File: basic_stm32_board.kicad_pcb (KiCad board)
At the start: 4 copper layers, 2 x 7.5 mm, 61 parts, among them J1 Screw_Terminal_01x02, J2 USB_B_Micro, J3 Conn_01x04, J4 Conn_01x04, J5 Conn_ARM_JTAG_SWD_10, Q1 AO3401A, SW1 SW_SPDT, U1 STM32F405RGT6, U2 MP2303ADN, U3 USBLC6-2SC6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

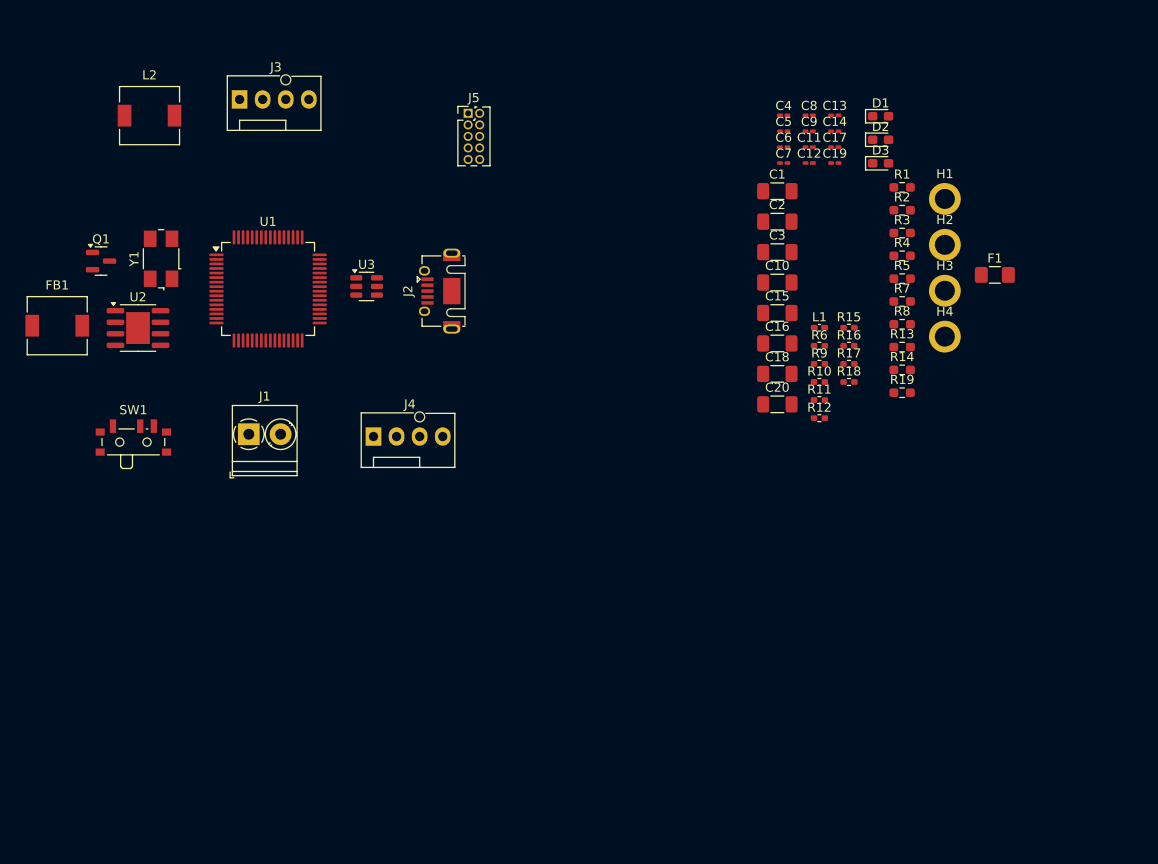
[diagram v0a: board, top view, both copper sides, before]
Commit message: changed some footprints
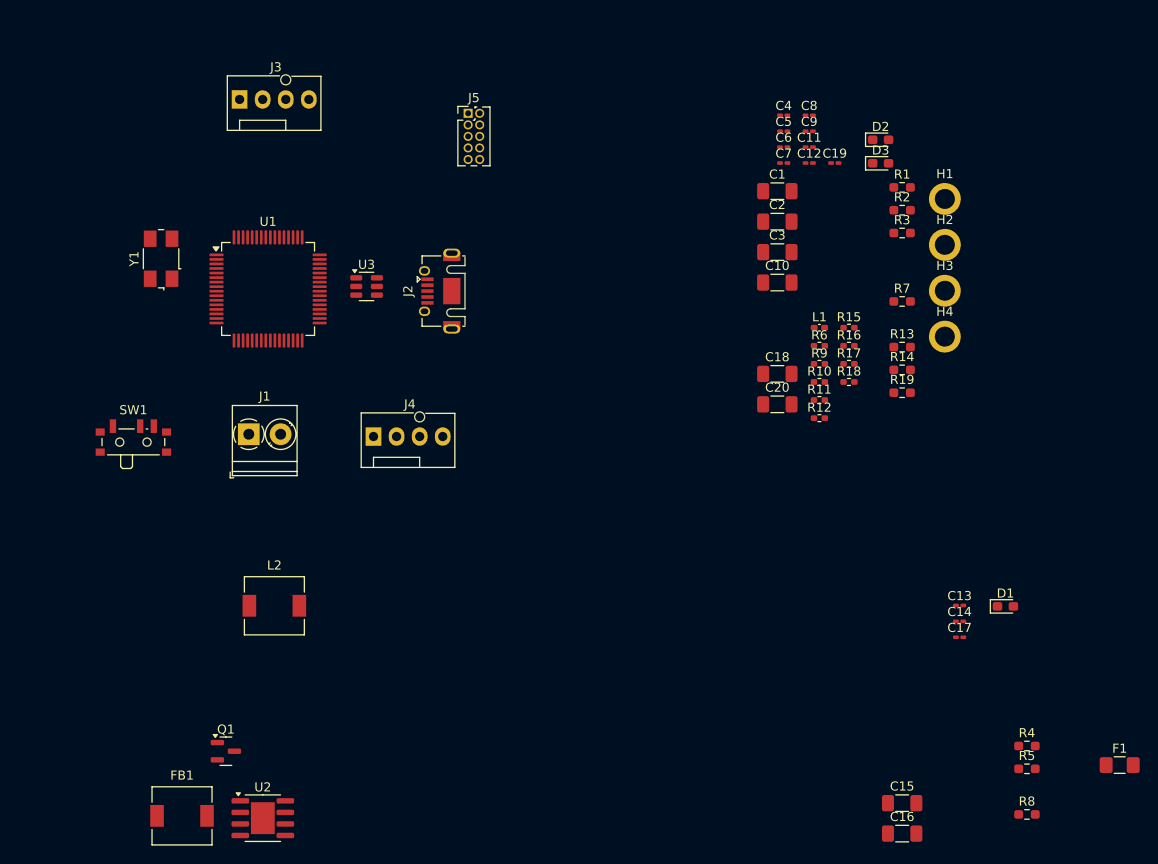
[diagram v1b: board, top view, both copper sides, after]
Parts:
- moved U2 55.6 mm to (156.2, 155.0)
- moved C13 55.6 mm to (232.9, 131.6)
- moved C14 55.6 mm to (232.9, 133.4)
- moved C15 55.6 mm to (226.6, 153.4)
- moved C17 55.6 mm to (232.9, 135.1)
- moved F1 55.6 mm to (250.5, 149.2)
- moved FB1 55.6 mm to (147.3, 154.8)
- moved Q1 55.6 mm to (152.2, 147.7)
- moved R4 55.6 mm to (240.3, 147.1)
- moved R5 55.6 mm to (240.3, 149.6)
- moved R8 55.6 mm to (240.3, 154.6)
- moved C16 55.6 mm to (226.6, 156.7)
- moved D1 55.6 mm to (237.9, 131.7)
- moved L2 55.6 mm to (157.5, 131.7)
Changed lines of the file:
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@@
 	(footprint "Inductor_SMD:L_6.3x6.3_H3"
 		(layer "F.Cu")
-		(at 133.604 100.838)
+		(at 147.3375 154.766)
 		(descr "Choke, SMD, 6.3x6.3mm 3mm height")
 		(tags "Choke SMD")
@@
 	(footprint "Inductor_SMD:L_6.3x6.3_H3"
 		(layer "F.Cu")
-		(at 143.764 77.724)
+		(at 157.4975 131.652)
 		(descr "Choke, SMD, 6.3x6.3mm 3mm height")
 		(tags "Choke SMD")
@@
 		(tags "Micro AB USB SMD")
 		(property "Reference" "J2"
-			(at 0 -4.8 270)
+			(at 0 -4.8 -90)
 			(layer "F.SilkS")
 			(effects
@@
 		)
 		(property "Value" "USB_B_Micro"
-			(at 0 3.5 270)
+			(at 0 3.5 -90)
 			(layer "F.Fab")
 			(effects
@@
 		)
 		(fp_text user "PCB Edge"
-			(at 0 1.45 270)
+			(at 0 1.45 -90)
 			(layer "Dwgs.User")
 			(effects
@@
 		)
 		(fp_text user "${REFERENCE}"
-			(at 0 -1.5 270)
+			(at 0 -1.5 -90)
 			(layer "F.Fab")
 			(effects
@@
 	(footprint "Capacitor_SMD:C_1206_3216Metric_Pad1.33x1.80mm_HandSolder"
 		(layer "F.Cu")
-		(at 212.8345 102.79)
+		(at 226.568 156.718)
 		(descr "Capacitor SMD 1206 (3216 Metric), square (rectangular) end terminal, IPC_7351 nominal with elongated pad for handsoldering. (Body size source: IPC-SM-782 page 76, https://www.pcb-3d.com/wordpress/wp-content/uploads/ipc-sm-782a_amendment_1_and_2.pdf), generated with kicad-footprint-generator")
 		(tags "capacitor handsolder")
@@
 	(footprint "Capacitor_SMD:C_0201_0603Metric_Pad0.64x0.40mm_HandSolder"
 		(layer "F.Cu")
-		(at 219.1545 77.69)
+		(at 232.888 131.618)
 		(descr "Capacitor SMD 0201 (0603 Metric), square (rectangular) end terminal, IPC_7351 nominal with elongated pad for handsoldering. (Body size source: https://www.vishay.com/docs/20052/crcw0201e3.pdf), generated with kicad-footprint-generator")
 		(tags "capacitor handsolder")
@@
 		(tags "SMD SMT crystal")
 		(property "Reference" "Y1"
-			(at 0 -2.95 270)
+			(at 0 -2.95 -90)
 			(layer "F.SilkS")
 			(effects
@@
 		)
 		(property "Value" "16MHz"
-			(at 0 2.95 270)
+			(at 0 2.95 -90)
 			(layer "F.Fab")
 			(effects
@@
 		)
 		(fp_text user "${REFERENCE}"
-			(at 0 0 270)
+			(at 0 0 -90)
 			(layer "F.Fab")
 			(effects
@@
 	(footprint "Capacitor_SMD:C_1206_3216Metric_Pad1.33x1.80mm_HandSolder"
 		(layer "F.Cu")
-		(at 212.8345 99.44)
+		(at 226.568 153.368)
 		(descr "Capacitor SMD 1206 (3216 Metric), square (rectangular) end terminal, IPC_7351 nominal with elongated pad for handsoldering. (Body size source: IPC-SM-782 page 76, https://www.pcb-3d.com/wordpress/wp-content/uploads/ipc-sm-782a_amendment_1_and_2.pdf), generated with kicad-footprint-generator")
 		(tags "capacitor handsolder")
@@
 	(footprint "Resistor_SMD:R_0603_1608Metric_Pad0.98x0.95mm_HandSolder"
 		(layer "F.Cu")
-		(at 226.5645 100.68)
+		(at 240.298 154.608)
 		(descr "Resistor SMD 0603 (1608 Metric), square (rectangular) end terminal, IPC_7351 nominal with elongated pad for handsoldering. (Body size source: IPC-SM-782 page 72, https://www.pcb-3d.com/wordpress/wp-content/uploads/ipc-sm-782a_amendment_1_and_2.pdf), generated with kicad-footprint-generator")
 		(tags "resistor handsolder")
@@
 	(footprint "Resistor_SMD:R_0603_1608Metric_Pad0.98x0.95mm_HandSolder"
 		(layer "F.Cu")
-		(at 226.5645 93.15)
+		(at 240.298 147.078)
 		(descr "Resistor SMD 0603 (1608 Metric), square (rectangular) end terminal, IPC_7351 nominal with elongated pad for handsoldering. (Body size source: IPC-SM-782 page 72, https://www.pcb-3d.com/wordpress/wp-content/uploads/ipc-sm-782a_amendment_1_and_2.pdf), generated with kicad-footprint-generator")
 		(tags "resistor handsolder")
@@
 	(footprint "Package_TO_SOT_SMD:SOT-23"
 		(layer "F.Cu")
-		(at 138.43 93.726)
+		(at 152.1635 147.654)
 		(descr "SOT, 3 Pin (https://www.jedec.org/system/files/docs/to-236h.pdf variant AB), generated with kicad-footprint-generator ipc_gullwing_generator.py")
 		(tags "SOT TO_SOT_SMD")
@@
 	(footprint "Diode_SMD:D_0603_1608Metric_Pad1.05x0.95mm_HandSolder"
 		(layer "F.Cu")
-		(at 224.1995 77.79)
+		(at 237.933 131.718)
 		(descr "Diode SMD 0603 (1608 Metric), square (rectangular) end terminal, IPC_7351 nominal, (Body size source: http://www.tortai-tech.com/upload/download/2011102023233369053.pdf), generated with kicad-footprint-generator")
 		(tags "diode handsolder")
@@
 	(footprint "Fuse:Fuse_1206_3216Metric_Pad1.42x1.75mm_HandSolder"
 		(layer "F.Cu")
-		(at 236.7645 95.25)
+		(at 250.498 149.178)
 		(descr "Fuse SMD 1206 (3216 Metric), square (rectangular) end terminal, IPC_7351 nominal with elongated pad for handsoldering. (Body size source: http://www.tortai-tech.com/upload/download/2011102023233369053.pdf), generated with kicad-footprint-generator")
 		(tags "fuse handsolder")
@@
 	(footprint "Resistor_SMD:R_0603_1608Metric_Pad0.98x0.95mm_HandSolder"
 		(layer "F.Cu")
-		(at 226.5645 95.66)
+		(at 240.298 149.588)
 		(descr "Resistor SMD 0603 (1608 Metric), square (rectangular) end terminal, IPC_7351 nominal with elongated pad for handsoldering. (Body size source: IPC-SM-782 page 72, https://www.pcb-3d.com/wordpress/wp-content/uploads/ipc-sm-782a_amendment_1_and_2.pdf), generated with kicad-footprint-generator")
 		(tags "resistor handsolder")
@@
 	(footprint "Capacitor_SMD:C_0201_0603Metric_Pad0.64x0.40mm_HandSolder"
 		(layer "F.Cu")
-		(at 219.1545 81.19)
+		(at 232.888 135.118)
 		(descr "Capacitor SMD 0201 (0603 Metric), square (rectangular) end terminal, IPC_7351 nominal with elongated pad for handsoldering. (Body size source: https://www.vishay.com/docs/20052/crcw0201e3.pdf), generated with kicad-footprint-generator")
 		(tags "capacitor handsolder")
@@
 	(footprint "Capacitor_SMD:C_0201_0603Metric_Pad0.64x0.40mm_HandSolder"
 		(layer "F.Cu")
-		(at 219.1545 79.44)
+		(at 232.888 133.368)
 		(descr "Capacitor SMD 0201 (0603 Metric), square (rectangular) end terminal, IPC_7351 nominal with elongated pad for handsoldering. (Body size source: https://www.vishay.com/docs/20052/crcw0201e3.pdf), generated with kicad-footprint-generator")
 		(tags "capacitor handsolder")
@@
 	(footprint "Package_SO:SOIC-8-1EP_3.9x4.9mm_P1.27mm_EP2.62x3.51mm"
 		(layer "F.Cu")
-		(at 142.494 101.092)
+		(at 156.2275 155.02)
 		(descr "SOIC, 8 Pin (https://www.monolithicpower.com/en/documentview/productdocument/index/version/2/document_type/Datasheet/lang/en/sku/MP2303A/document_id/494#page=14), generated with kicad-footprint-generator ipc_gullwing_generator.py")
 		(tags "SOIC SO")

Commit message: Footprint placement changed
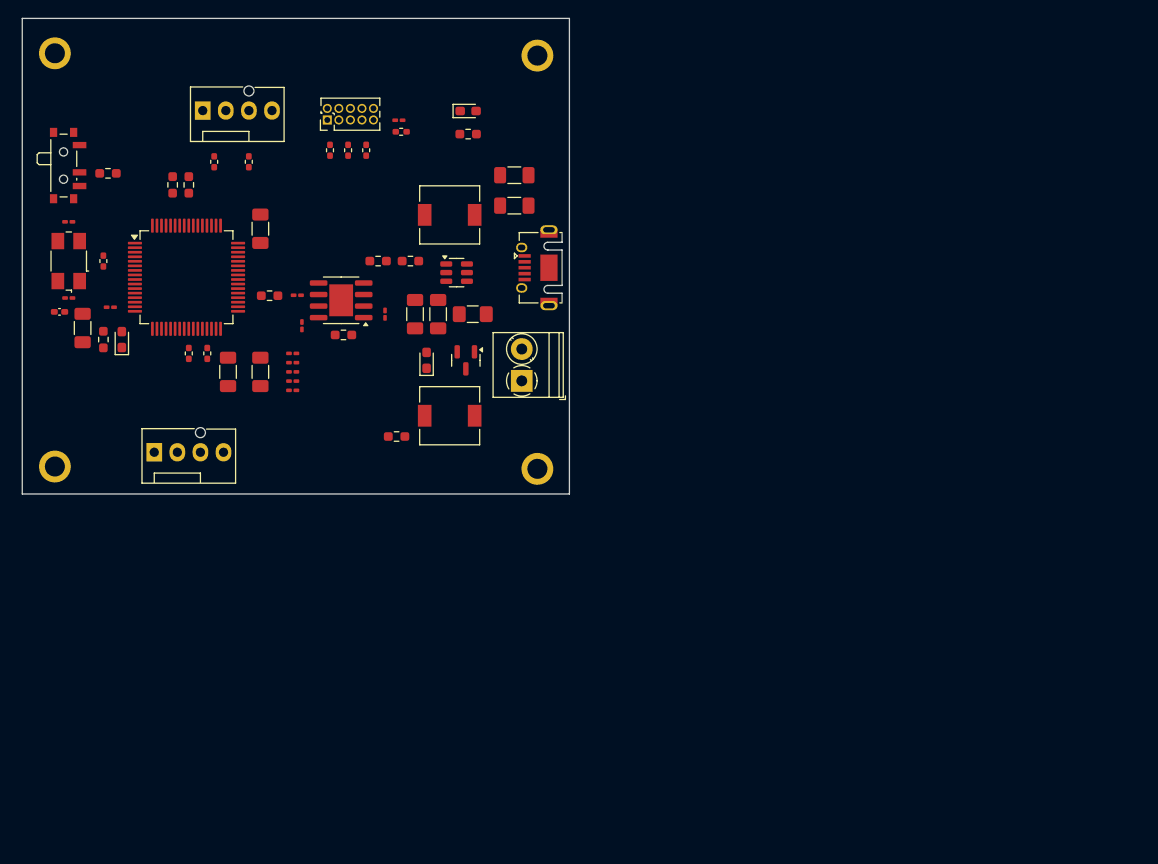
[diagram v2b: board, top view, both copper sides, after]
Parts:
- moved R8 101.0 mm to (157.0, 97.5)
- moved H2 100.2 mm to (133.3, 70.9)
- moved H4 99.0 mm to (133.3, 116.3)
- moved R1 89.5 mm to (138.7, 102.4), turned to 90 degrees
- moved R4 87.7 mm to (165.1, 101.9)
- moved R2 87.5 mm to (139.2, 84.1), turned to 180 degrees
- moved F1 86.8 mm to (179.3, 99.6), turned to 180 degrees
- moved D2 86.3 mm to (140.7, 102.4), turned to 90 degrees
- moved L1 83.6 mm to (133.9, 99.3)
- moved C9 83.5 mm to (134.9, 97.8), turned to 180 degrees
- moved C11 81.9 mm to (134.9, 89.4)
- moved R7 81.3 mm to (146.3, 85.3), turned to -90 degrees
- moved C13 80.5 mm to (160.0, 97.5)
- moved C14 79.3 mm to (160.5, 100.8), turned to -90 degrees
- moved R6 79.3 mm to (138.7, 93.7), turned to 90 degrees
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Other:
- board size 2 x 7.5 mm -> 60.2 x 52.3 mm

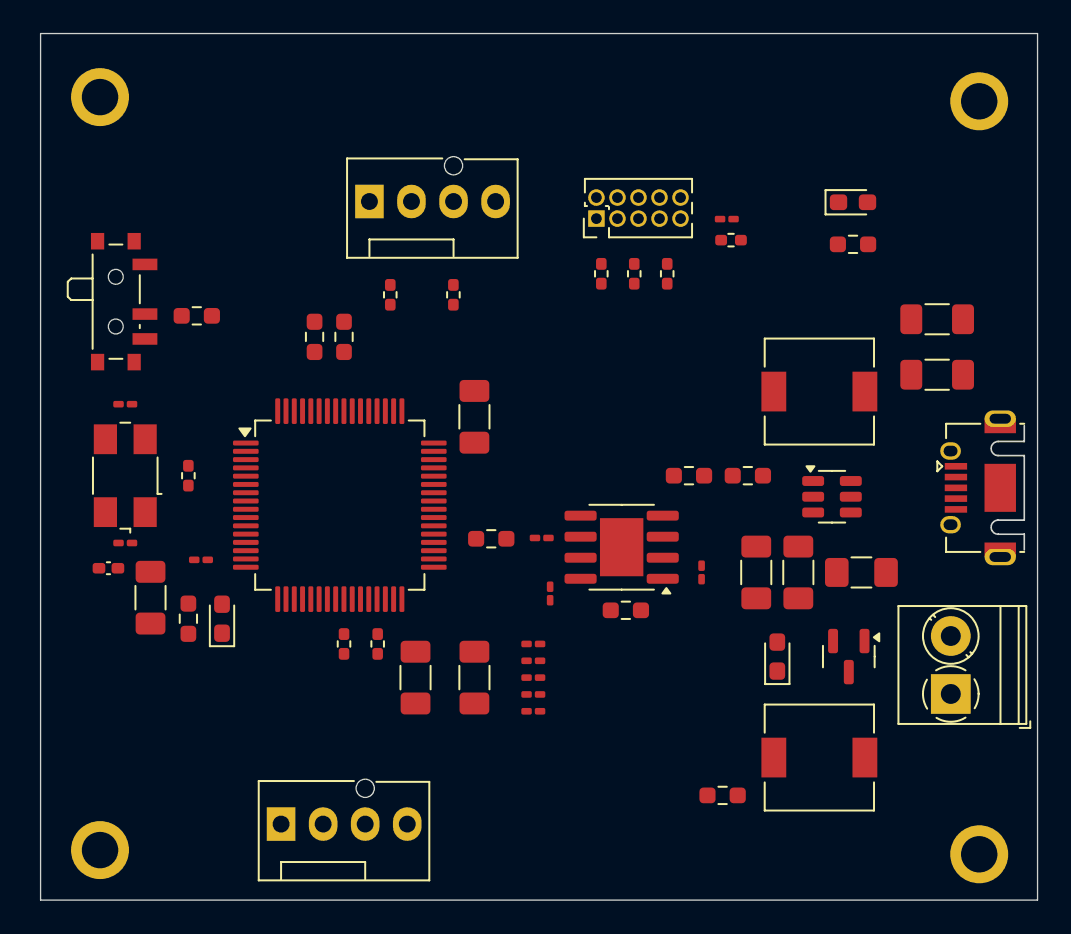
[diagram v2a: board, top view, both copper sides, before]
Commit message: added signal traces
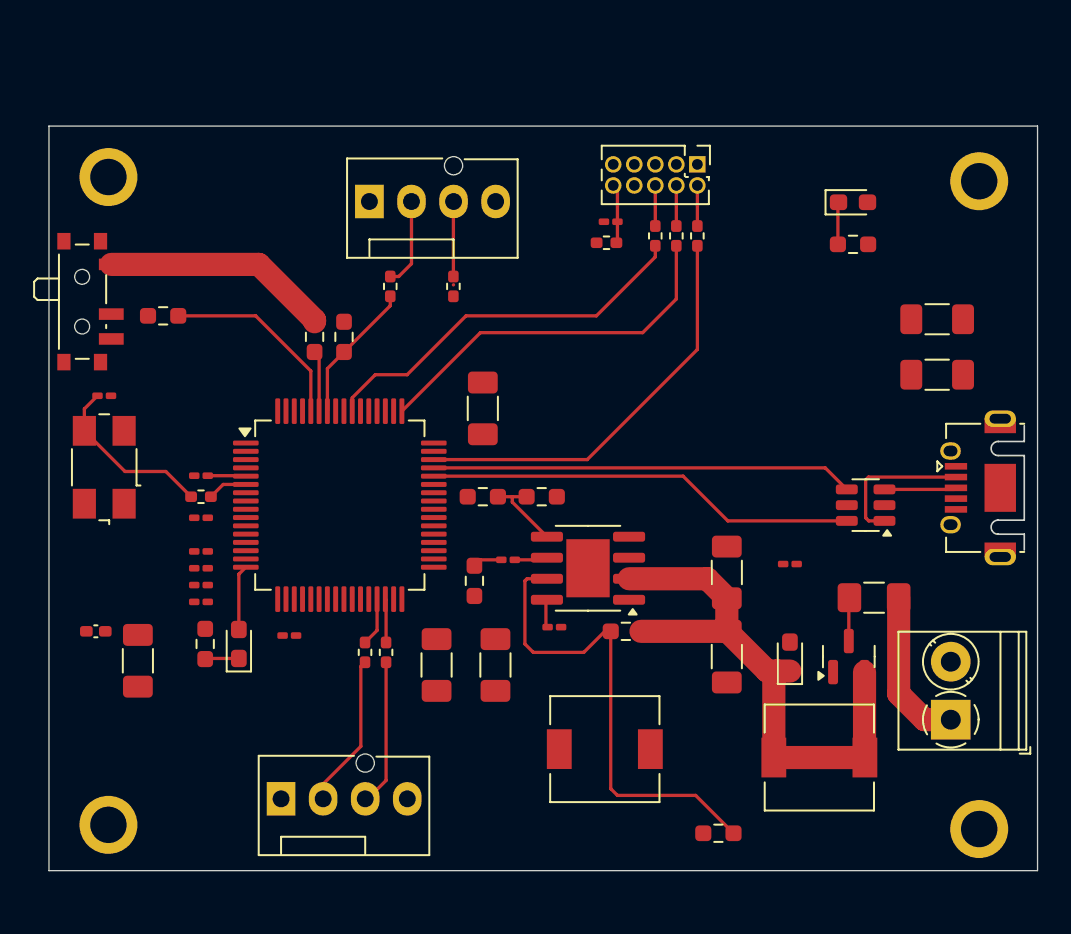
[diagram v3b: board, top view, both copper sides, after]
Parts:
- moved L2 25.2 mm to (163.8, 110.2), turned to 180 degrees
- moved C4 21.8 mm to (139.4, 96.3), turned to 180 degrees
- moved C6 21.5 mm to (139.4, 99.3), turned to 180 degrees
- moved C5 20.8 mm to (139.4, 100.3), turned to 180 degrees
- moved C8 20.8 mm to (139.4, 98.3), turned to 180 degrees
- moved C7 15.4 mm to (144.8, 103.4), turned to 180 degrees
- moved R13 12.5 mm to (160.0, 95.0)
- moved R14 12.5 mm to (156.5, 95.0)
- moved R18 7.52 mm to (163.9, 79.7)
- moved C19 7.01 mm to (164.2, 78.4), turned to 180 degrees
- moved J5 6.92 mm to (169.4, 74.9), turned to -90 degrees
- moved C9 6.12 mm to (139.4, 93.7)
- moved C15 5.38 mm to (171.2, 104.6)
- moved C17 5.36 mm to (175.0, 99.1), turned to 180 degrees
- moved R15 5.07 mm to (168.1, 79.2)
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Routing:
- net Buck_IN: track 0.00 -> 34.3 mm
- net Buck_EN: track 0.00 -> 29.1 mm
- net USB_D-: track 0.00 -> 26.1 mm
- net USB_D+: track 0.00 -> 25.5 mm
- net SWDIO: track 0.00 -> 24.9 mm
- net SWO: track 0.00 -> 23.3 mm
- net SWCLK: track 0.00 -> 22.6 mm
- net +3.3VA: track 0.00 -> 13.8 mm
- net BOOT0: track 0.00 -> 11.8 mm
- net Net-(C11-Pad1): track 0.00 -> 10.5 mm
- net P,+12: track 0.00 -> 9.60 mm
- net Net-(J4-Pin_2): track 0.00 -> 9.29 mm
- net USB_Conn_D-: track 0.00 -> 9.02 mm
- net Net-(J4-Pin_3): track 0.00 -> 8.86 mm
- net I2C1_SCL: track 0.00 -> 8.51 mm
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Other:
- board size 60.2 x 52.3 mm -> 59.7 x 45 mm
